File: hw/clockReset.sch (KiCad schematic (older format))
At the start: 6 parts

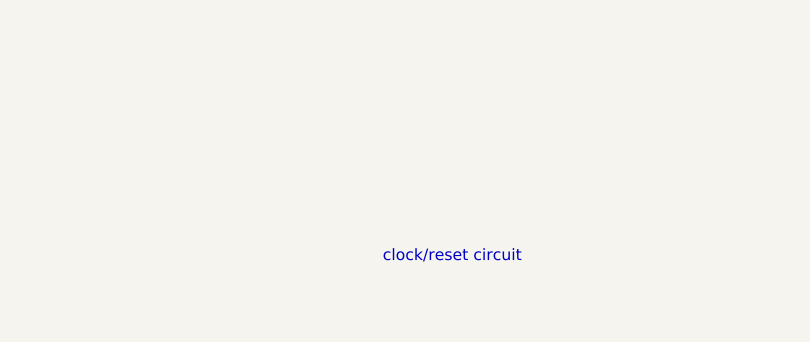
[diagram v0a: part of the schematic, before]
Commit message: minor tweaks, added sheet pins on main schematic?
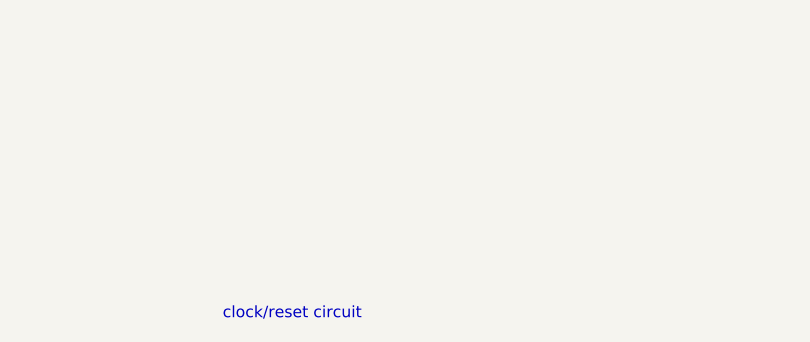
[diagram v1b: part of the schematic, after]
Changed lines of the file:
@@
 $Descr USLetter 11000 8500
 encoding utf-8
-Sheet 5 5
+Sheet 5 4
 Title ""
 Date ""
@@
 Text HLabel 7950 5000 2    50   Output ~ 0
 SCLK
-Text Notes 7050 6700 0    50   ~ 0
+Text Notes 6350 6950 0    50   ~ 0
 clock/reset circuit
 $EndSCHEMATC
